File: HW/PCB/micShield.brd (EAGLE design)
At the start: 37.8 x 26.7 mm, 19 parts, among them U2 LT6002CGN

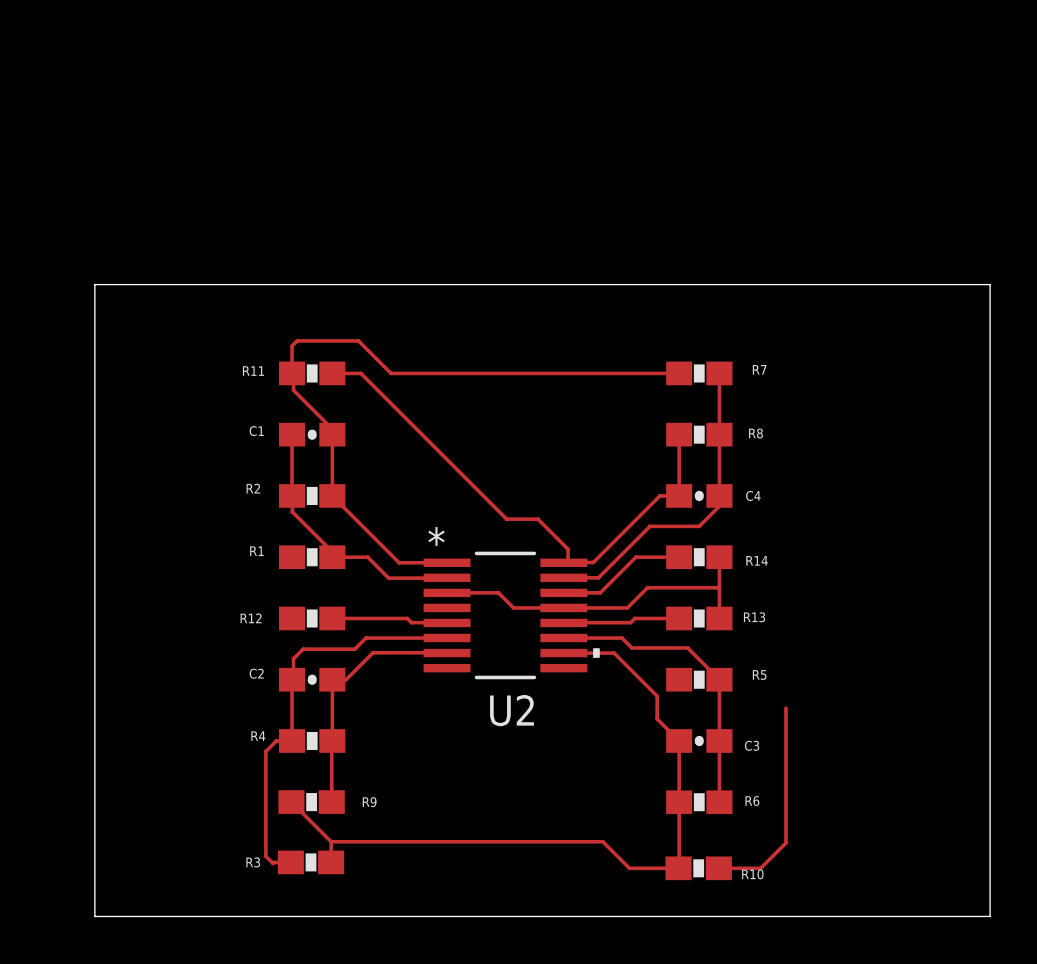
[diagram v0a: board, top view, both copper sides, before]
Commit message: Added Mic Library and updates to PCB.
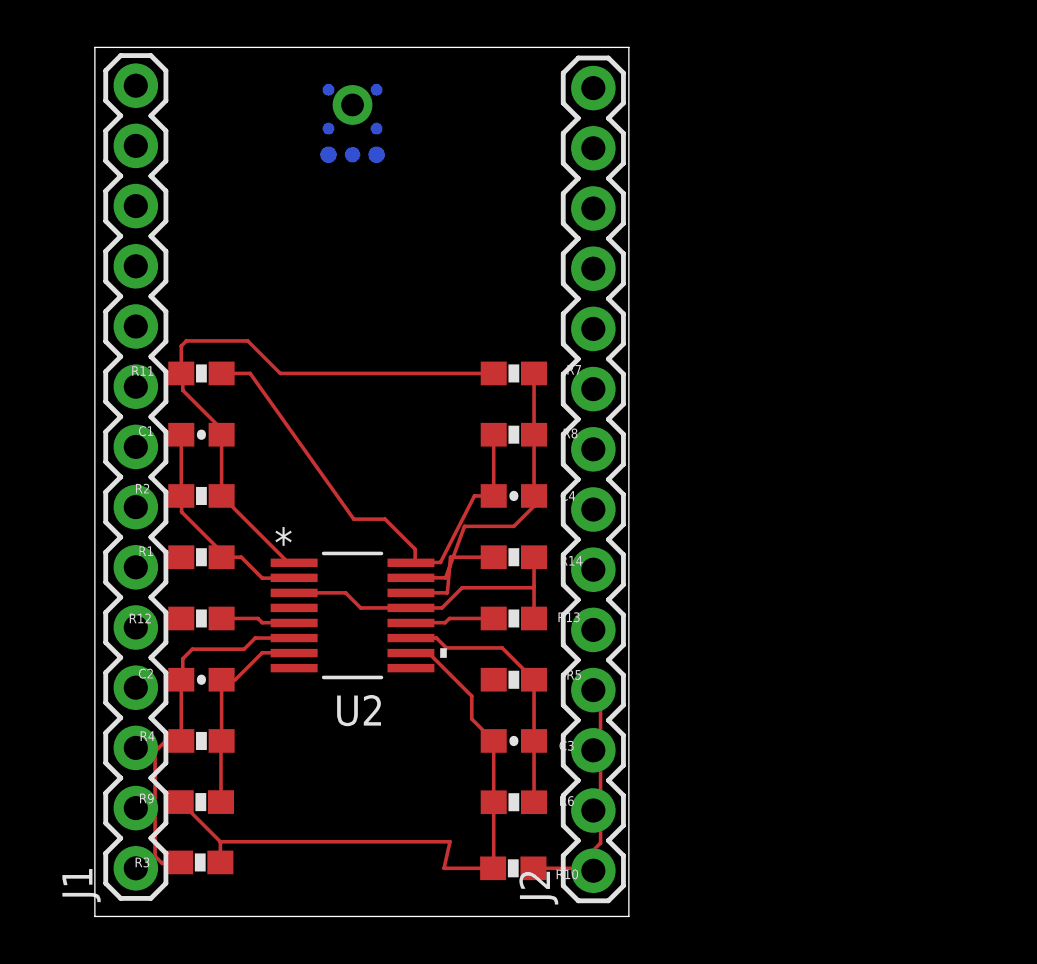
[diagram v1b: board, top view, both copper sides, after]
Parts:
- added J1, J2: (no value), SparkFun-Connectors:1X14
- added M1: PMM-3738-VM1010-R, MIC:PMM-3738-VM1010-R
- moved C3 7.82 mm to (17.7, 7.40)
- moved C4 7.82 mm to (17.7, 17.7)
- moved R10 7.82 mm to (17.7, 2.03)
- moved R13 7.82 mm to (17.7, 12.6)
- moved R14 7.82 mm to (17.7, 15.2)
- moved R5 7.82 mm to (17.7, 9.99)
- moved R6 7.82 mm to (17.7, 4.82)
- moved R7 7.82 mm to (17.7, 22.9)
- moved R8 7.82 mm to (17.7, 20.3)
- moved U2 6.45 mm to (10.9, 12.7)
- moved R3 4.67 mm to (4.45, 2.28)
- moved R9 4.67 mm to (4.47, 4.83)
- moved C1 4.67 mm to (4.50, 20.3)
- moved C2 4.67 mm to (4.50, 9.99)
- moved R1 4.67 mm to (4.50, 15.2)
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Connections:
- removed net +V: U2.4
- new net DOUT: M1.7
- new net GA1: M1.3
- new net GA2: M1.2
- new net MODE: M1.5
- new net V3_3: M1.6, U2.4
- net GND: now also M1.4, M1.8
- net TO_AMP: now also M1.1
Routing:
- net FILTER_1_OUT: track 30.0 -> 25.1 mm
- net FILTER_3_OUT: track 30.7 -> 27.1 mm
- net FILTER_2_OUT: track 31.2 -> 29.2 mm
- net N$3: track 17.2 -> 15.5 mm
- net FILTER_4_OUT: track 10.5 -> 8.72 mm
- net N$2: track 4.92 -> 3.14 mm
- net N$1: track 11.1 -> 9.31 mm
- net N$4: track 4.94 -> 3.57 mm
- net N$5: track 12.5 -> 11.1 mm
- net GND: track 14.7 -> 13.3 mm
- net N$7: track 13.4 -> 12.7 mm
- net N$8: track 5.49 -> 4.87 mm
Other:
- board size 37.8 x 26.7 mm -> 22.5 x 36.7 mm

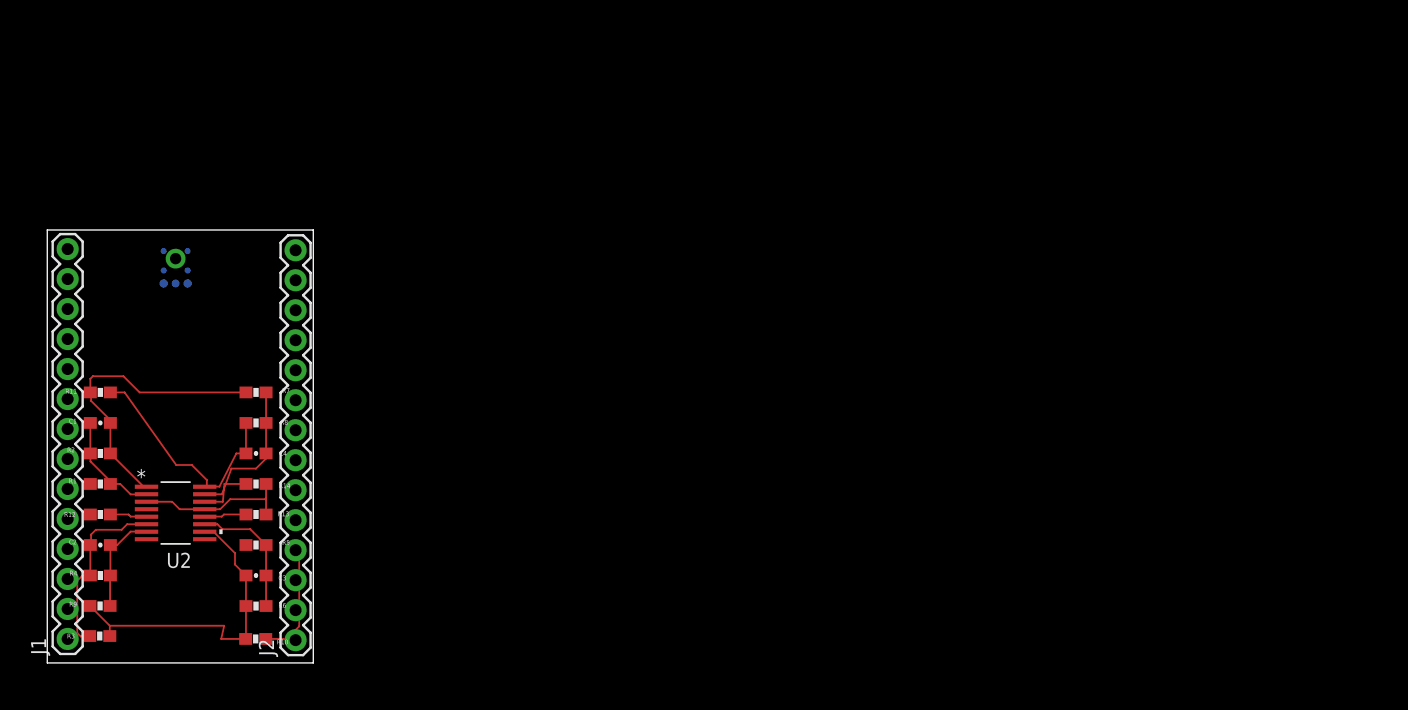
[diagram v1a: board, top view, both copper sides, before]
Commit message: Adding libs. Working on analog front end.
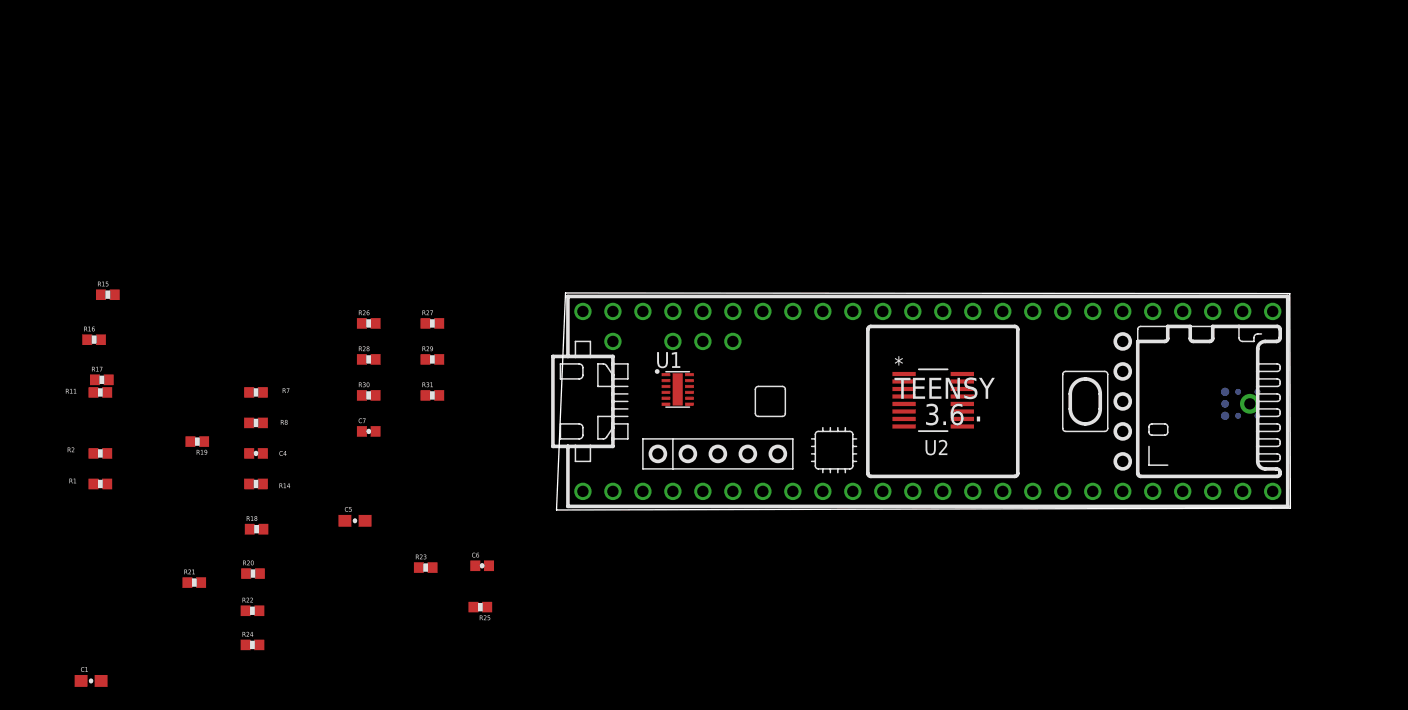
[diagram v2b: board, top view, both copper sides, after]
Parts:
- removed C2, C3: (no value), SparkFun-Capacitors:0603-CAP
- removed J1, J2: (no value), SparkFun-Connectors:1X14
- removed R10, R12, R13, R3, R4, R5, R6, R9: (no value), SparkFun-Passives:0603-RES
- added C5: (no value), SparkFun-Capacitors:0603-CAP
- added C6: 0.1uF, SparkFun-Capacitors:0402-CAP
- added C7: 0,1uF, SparkFun-Capacitors:0402-CAP
- added R15, R16, R17: (no value), SparkFun-Resistors:0402-RES
- added R18, R22, R24, R28, R30: DNP, SparkFun-Resistors:0402-RES
- added R19, R20, R25, R26, R31: 0, SparkFun-Resistors:0402-RES
- added R21, R27: 3.9k, SparkFun-Resistors:0402-RES
- added R23, R29: 3k, SparkFun-Resistors:0402-RES
- added U$1: TEENSY_3.5/3.6_BASIC, Teensy356:TEENSY_3.5/3.6_BASIC
- added U1: LM27762DSSR, LM27762DSSR:SON50P300X200X80-12N
- C4: value (none) -> 0.1uF; device SparkFun-Capacitors:0603-CAP -> SparkFun-Capacitors:0402-CAP
- R1, R2: device SparkFun-Passives:0603-RES -> SparkFun-Resistors:0402-RES
- R11: value (none) -> DNP; device SparkFun-Passives:0603-RES -> SparkFun-Resistors:0402-RES
- R14: value (none) -> 3k; device SparkFun-Passives:0603-RES -> SparkFun-Resistors:0402-RES
- R7: value (none) -> 0; device SparkFun-Passives:0603-RES -> SparkFun-Resistors:0402-RES
- R8: value (none) -> 3.9k; device SparkFun-Passives:0603-RES -> SparkFun-Resistors:0402-RES
- moved M1 91.8 mm to (101.9, 21.9), turned to 180 degrees
- moved U2 64.9 mm to (75.0, 22.3)
- moved C1 21.9 mm to (3.71, -1.52)
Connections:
- removed net FILTER_1_OUT: C1.2, R11.1, R2.2, R7.1, U2.1
- removed net FILTER_2_OUT: C4.2, R10.1, R11.2, R5.1, R8.2, U2.16
- removed net FILTER_3_OUT: C3.2, R10.2, R3.1, R6.2, R9.1, U2.10
- removed net FILTER_4_OUT: C2.2, R4.2, R9.2, U2.7
- removed net N$2: R12.2, U2.5
- removed net N$3: C2.1, R3.2, R4.1, U2.6
- removed net N$4: R13.2, U2.12
- removed net N$5: C3.1, R5.2, R6.1, U2.11
- removed net N$8: R14.2, U2.14
- removed net V3_3: M1.6, U2.4
- new net F1_OUT: R11.2, R19.2, R26.1, R28.1
- new net F2_OUT: R20.1, R22.1, R28.2, R31.2
- new net FILTERED_OUT: R22.2, R25.2
- new net N$10: C4.2, R19.1, R8.2, U2.16
- new net N$12: R20.2, R24.2, U2.11
- new net N$13: C6.1, R21.1, R23.2, U2.12
- new net N$14: C6.2, R21.2, R25.1, U2.10
- new net N$16: R26.2, R30.2, U2.6
- new net N$17: C7.1, R27.1, R29.2, U2.5
- new net N$18: C7.2, R27.2, R31.1, U2.7
- new net N$6: R15.2, R16.1, R17.1, U2.3
- new net N$9: R18.2, R7.2, U2.14
- new net OFFSET_REMOVED: R11.1, R2.2, R7.1, U2.1
- new net V3_3N: C1.1, U2.13
- new net V3_3P: C5.1, M1.6, R15.1, U2.4
- net GND: now also C1.2, C5.2, R16.2, R17.2, R18.1, R23.1, R24.1, R29.1, R30.1, U1.4; no longer R12.1, R13.1, U2.13, U2.3
- net N$1: no longer C1.1
- net N$7: now also R14.2; no longer R7.2
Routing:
- net FILTER_2_OUT: track 29.2 -> 0.00 mm
- net FILTER_3_OUT: track 27.1 -> 0.00 mm
- net FILTER_1_OUT: track 25.1 -> 0.00 mm
- net N$3: track 15.5 -> 0.00 mm
- net GND: track 13.3 -> 0.00 mm
- net N$7: track 12.7 -> 0.00 mm
- net N$5: track 11.1 -> 0.00 mm
- net N$1: track 9.31 -> 0.00 mm
- net FILTER_4_OUT: track 8.72 -> 0.00 mm
- net N$8: track 4.87 -> 0.00 mm
- net N$4: track 3.57 -> 0.00 mm
- net N$2: track 3.14 -> 0.00 mm
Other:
- board size 22.5 x 36.7 mm -> 62.2 x 18.4 mm

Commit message: More updates to the PCB. Added +/-3V
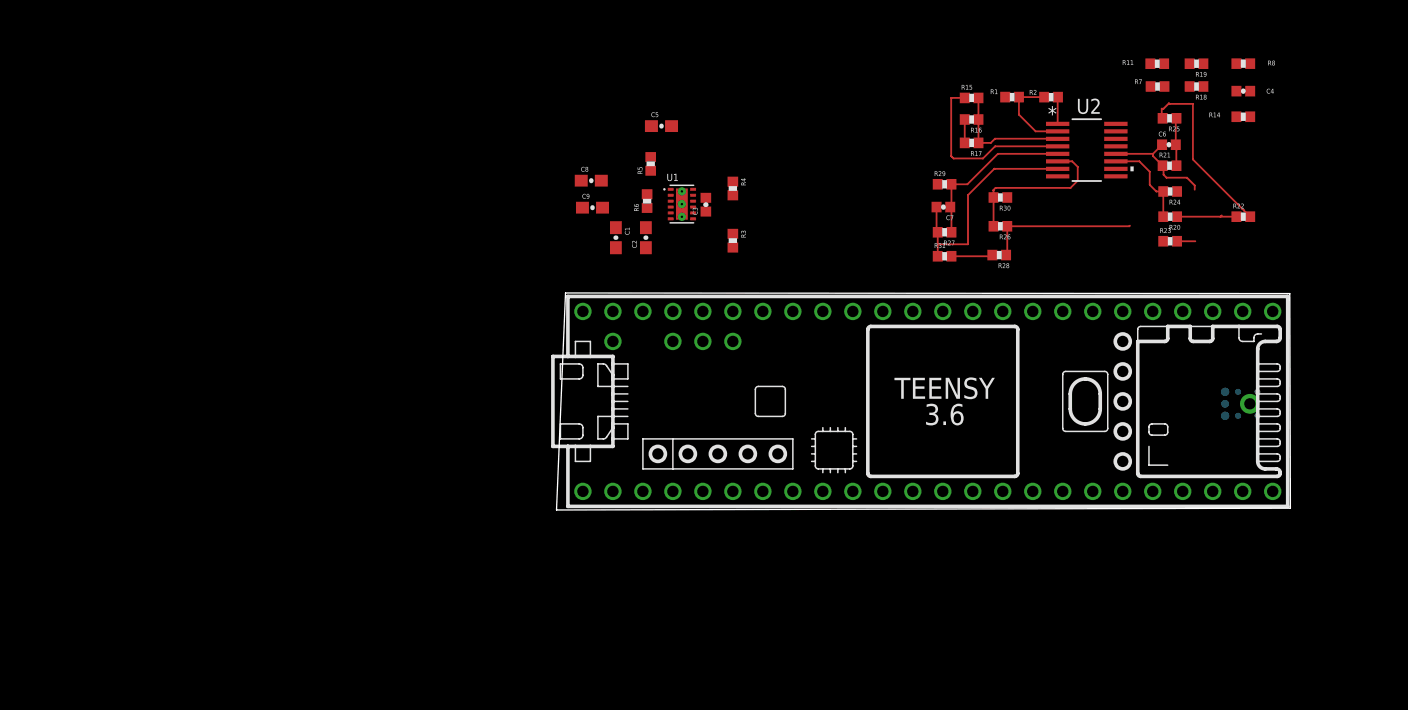
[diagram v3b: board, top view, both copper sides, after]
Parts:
- added C2, C8, C9: (no value), SparkFun-Capacitors:0603-CAP
- added C3: (no value), SparkFun-Capacitors:0402-CAP
- added R3, R5: 866k, SparkFun-Resistors:0402-RES
- added R4, R6: 499k, SparkFun-Resistors:0402-RES
- U1: device LM27762DSSR:SON50P300X200X80-12N -> LM27762DSSR:VREG_LM27762DSSR
- moved R11 93.7 mm to (94.0, 50.7)
- moved R19 90.5 mm to (97.3, 50.7)
- moved R22 90.3 mm to (101.3, 37.8)
- moved R21 89.8 mm to (95.0, 42.1)
- moved R14 89.2 mm to (101.3, 46.3), turned to 0 degrees
- moved C4 89.1 mm to (101.3, 48.4)
- moved R8 89.0 mm to (101.3, 50.8)
- moved R18 88.0 mm to (97.3, 48.8), turned to 180 degrees
- moved R24 86.7 mm to (95.1, 39.9), turned to 180 degrees
- moved R2 86.0 mm to (85.0, 47.9)
- moved R1 83.9 mm to (81.7, 47.9)
- moved R20 83.3 mm to (95.1, 37.8), turned to 180 degrees
- moved R7 80.6 mm to (94.0, 48.8)
- moved R16 76.6 mm to (78.3, 46.0), turned to 180 degrees
- moved R17 76.3 mm to (78.3, 44.0), turned to 180 degrees
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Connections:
- new net 5V: U1.12, U1.3, U1.8
- new net FB_N: R3.1, R4.2, U1.7
- new net FB_P: R5.1, R6.2, U1.2
- new net N$2: C2.2, U1.5
- new net N$3: C3.1, U1.9
- new net N$4: C3.2, U1.10
- net GND: now also C2.1, C8.1, C9.1, R4.1, R6.1, U1.1, U1.13, U1.13.1, U1.13.2, U1.13.3
- net V3_3N: now also C9.2, R3.2, U1.6
- net V3_3P: now also C8.2, R5.2, U1.11
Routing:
- net N$18: track 0.00 -> 19.7 mm
- net V3_3P: track 0.00 -> 15.6 mm
- net FILTERED_OUT: track 0.00 -> 15.3 mm
- net N$17: track 0.00 -> 14.3 mm
- net N$16: track 0.00 -> 13.6 mm
- net F1_OUT: track 0.00 -> 12.9 mm
- net N$13: track 0.00 -> 11.3 mm
- net N$6: track 0.00 -> 10.7 mm
- net F2_OUT: track 0.00 -> 8.69 mm
- net N$12: track 0.00 -> 7.86 mm
- net N$1: track 0.00 -> 7.50 mm
- net N$14: track 0.00 -> 4.06 mm
- net OFFSET_REMOVED: track 0.00 -> 2.27 mm
- net GND: track 0.00 -> 1.98 mm

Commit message: Routing updates.
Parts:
- moved M1 31.9 mm to (93.6, 52.8)
- moved R2 13.5 mm to (72.6, 42.6), turned to 180 degrees
- moved R22 12.5 mm to (88.8, 39.3), turned to 180 degrees
- moved R7 11.8 mm to (85.0, 41.3)
- moved R11 11.7 mm to (85.0, 43.4)
- moved R1 11.7 mm to (72.6, 40.7)
- moved R28 11.5 mm to (69.2, 35.4)
- moved C4 11.4 mm to (92.5, 41.3)
- moved R27 11.4 mm to (64.9, 38.8)
- moved R18 11.4 mm to (88.8, 41.3)
- moved C7 11.3 mm to (64.8, 40.7)
- moved R29 11.3 mm to (64.9, 42.6)
- moved R31 11.3 mm to (64.9, 36.5)
- moved R8 11.3 mm to (92.7, 43.4)
- moved R19 11.2 mm to (88.8, 43.4)
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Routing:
- net V3_3N: track 0.00 -> 24.6 mm, vias 0 -> 1
- net F2_OUT: track 8.69 -> 32.8 mm
- net N$7: track 0.00 -> 19.4 mm, vias 0 -> 2
- net N$10: track 0.00 -> 18.3 mm, vias 0 -> 2
- net OFFSET_REMOVED: track 2.27 -> 19.8 mm
- net F1_OUT: track 12.9 -> 29.5 mm, vias 0 -> 2
- net GND: track 1.98 -> 17.8 mm, vias 0 -> 2
- net N$14: track 4.06 -> 16.3 mm, vias 0 -> 3
- net N$9: track 0.00 -> 8.68 mm
- net FILTERED_OUT: track 15.3 -> 6.79 mm
- net N$16: track 13.6 -> 5.19 mm
- net N$13: track 11.3 -> 17.4 mm, vias 0 -> 2
- net TO_AMP: track 0.00 -> 3.51 mm
- net N$17: track 14.3 -> 17.4 mm
- net N$12: track 7.86 -> 10.1 mm
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
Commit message: Schematics and Layout updates.
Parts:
- added C10: (no value), SparkFun-Capacitors:0603-CAP
- added R10, R9: (no value), SparkFun-Resistors:0402-RES
- moved M1 32.4 mm to (102.9, 21.7), flipped to the bottom, turned to 0 degrees
- moved C5 29.3 mm to (61.1, 17.6), flipped to the bottom, turned to 180 degrees
- moved R8 26.0 mm to (95.4, 17.6), flipped to the bottom, turned to 0 degrees
- moved R19 25.9 mm to (91.5, 17.6), flipped to the bottom, turned to 0 degrees
- moved R11 25.9 mm to (87.6, 17.6), flipped to the bottom, turned to 180 degrees
- moved R5 25.2 mm to (58.3, 18.1), flipped to the bottom
- moved C8 24.9 mm to (61.0, 20.9), flipped to the bottom
- moved R15 24.4 mm to (71.8, 18.3), flipped to the bottom, turned to 180 degrees
- moved R2 24.4 mm to (75.2, 18.3), flipped to the bottom, turned to 0 degrees
- moved R29 24.4 mm to (67.5, 18.3), flipped to the bottom, turned to 180 degrees
- moved R6 22.1 mm to (55.8, 17.6), flipped to the bottom, turned to 180 degrees
- moved R7 21.8 mm to (87.6, 19.7), flipped to the bottom, turned to 180 degrees
- moved C4 21.8 mm to (95.1, 19.7), flipped to the bottom, turned to 0 degrees
- moved R18 21.8 mm to (91.5, 19.7), flipped to the bottom, turned to 0 degrees
- moved C7 20.6 mm to (67.4, 20.3), flipped to the bottom, turned to 0 degrees
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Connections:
- new net N$11: R10.2, U$1.VIN
- new net N$5: R9.2, U$1.VUSB
- net 5V: now also C10.2, R10.1, R9.1
- net FILTERED_OUT: now also U$1.14/A0
- net GND: now also C10.1, U$1.AGND, U$1.GND, U$1.GND2
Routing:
- net GND: track 17.8 -> 33.8 mm
- net 5V: track 0.00 -> 15.5 mm, vias 0 -> 3
- net V3_3P: track 16.2 -> 28.5 mm
- net N$11: track 0.00 -> 10.8 mm
- net FB_P: track 0.00 -> 9.13 mm
- net N$5: track 0.00 -> 8.26 mm
- net FB_N: track 0.00 -> 3.74 mm
- net TO_AMP: track 3.51 -> 0.00 mm
- net N$4: track 0.00 -> 1.75 mm
- net N$3: track 0.00 -> 1.71 mm
- net N$2: track 0.00 -> 1.66 mm
- net V3_3N: track 24.6 -> 23.5 mm, vias 1 -> 2
- net OFFSET_REMOVED: track 19.8 -> 19.2 mm
- added copper zone on layer 1, net GND
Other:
- board size 62.2 x 18.4 mm -> 61.4 x 18.2 mm

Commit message: More updates to schematics and layout.
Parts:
- added R12: (no value), SparkFun-Resistors:0402-RES
- moved M1 1.77 mm to (101.1, 22.1)
- flipped R10 to the bottom
- flipped R9 to the bottom
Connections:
- net DOUT: now also U$1.34/A15
- net GA1: now also R12.1
- net GA2: now also R12.2
- net MODE: now also U$1.33/A14
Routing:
- net V3_3P: track 28.5 -> 78.8 mm, vias 0 -> 1
- net TO_AMP: track 0.00 -> 31.6 mm, vias 0 -> 1
- net V3_3N: track 23.5 -> 48.0 mm
- net FILTERED_OUT: track 6.79 -> 26.0 mm, vias 0 -> 2
- net DOUT: track 0.00 -> 10.2 mm, vias 0 -> 1
- net 5V: track 15.5 -> 24.2 mm
- net MODE: track 0.00 -> 8.13 mm
- net N$14: track 16.3 -> 19.0 mm
- net GA2: track 0.00 -> 2.25 mm
- net GA1: track 0.00 -> 2.22 mm
- net GND: vias 2 -> 14
- added copper zone on layer 16, net GND
